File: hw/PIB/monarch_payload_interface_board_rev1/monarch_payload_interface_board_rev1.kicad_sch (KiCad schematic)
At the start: 0 parts

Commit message: Components selection for valves so far
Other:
- added sheet MCU (MCU.kicad_sch)
- added sheet PC104_stack (PC104_stack.kicad_sch)
- added sheet Valves (valves.kicad_sch)
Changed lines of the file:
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@@
 	(generator_version "9.0")
 	(paper "A4")
+	(sheet
+		(at 106.68 52.07)
+		(size 111.76 17.78)
+		(exclude_from_sim no)
+		(in_bom yes)
+		(on_board yes)
+		(dnp no)
+		(stroke
+			(width 0.1524)
+			(type solid)
+		)
+		(fill
+			(color 0 0 0 0.0000)
+		)
+		(property "Sheetname" "MCU"
+			(at 106.68 51.3584 0)
+			(effects
+				(font
+					(size 1.27 1.27)
+				)
+				(justify left bottom)
+			)
+		)
+		(property "Sheetfile" "MCU.kicad_sch"
+			(at 113.284 50.038 0)
+			(effects
+				(font
+					(size 1.27 1.27)
+				)
+				(justify left top)
+			)
+		)
+		(instances
+			(project "monarch_payload_interface_board_rev1"
+				(path "/bf7ee58d-ac53-49d1-a6b2-96a87d67b737"
+					(page "3")
+				)
+			)
+		)
+	)
+	(sheet
+		(at 62.23 52.07)
+		(size 34.29 80.01)
+		(exclude_from_sim no)
+		(in_bom yes)
+		(on_board yes)
+		(dnp no)
+		(fields_autoplaced yes)
+		(stroke
+			(width 0.1524)
+			(type solid)
+		)
+		(fill
+			(color 0 0 0 0.0000)
+		)
+		(property "Sheetname" "PC104_stack"
+			(at 62.23 51.3584 0)
+			(effects
+				(font
+					(size 1.27 1.27)
+				)
+				(justify left bottom)
+			)
+		)
+		(property "Sheetfile" "PC104_stack.kicad_sch"
+			(at 62.23 132.6646 0)
+			(effects
+				(font
+					(size 1.27 1.27)
+				)
+				(justify left top)
+			)
+		)
+		(instances
+			(project "monarch_payload_interface_board_rev1"
+				(path "/bf7ee58d-ac53-49d1-a6b2-96a87d67b737"
+					(page "2")
+				)
+			)
+		)
+	)
+	(sheet
+		(at 125.73 92.71)
+		(size 72.39 34.29)
+		(exclude_from_sim no)
+		(in_bom yes)
+		(on_board yes)
+		(dnp no)
+		(fields_autoplaced yes)
+		(stroke
+			(width 0.1524)
+			(type solid)
+		)
+		(fill
+			(color 0 0 0 0.0000)
+		)
+		(property "Sheetname" "Valves"
+			(at 125.73 91.9984 0)
+			(effects
+				(font
+					(size 1.27 1.27)
+				)
+				(justify left bottom)
+			)
+		)
+		(property "Sheetfile" "valves.kicad_sch"
+			(at 125.73 127.5846 0)
+			(effects
+				(font
+					(size 1.27 1.27)
+				)
+				(justify left top)
+			)
+		)
+		(instances
+			(project "monarch_payload_interface_board_rev1"
+				(path "/bf7ee58d-ac53-49d1-a6b2-96a87d67b737"
+					(page "4")
+				)
+			)
+		)
+	)
 	(sheet_instances
 		(path "/"

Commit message: More components
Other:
- added sheet 12V Power Supply (power supply.kicad_sch)
- added sheet TCs (thermocouples.kicad_sch)
- sheet MCU ports: added 3V3, GND, I2C1_SCL, I2C1_SDA, I2C2_SCL, I2C2_SDA, I2C3_SCL, I2C3_SDA, I2C4_SCL, I2C4_SDA, SPI3_MISO, SPI3_MOSI, SPI3_SCK, UART_RX, UART_TX, Valve1, Valve10, Valve11, Valve12, Valve13, Valve14, Valve15, Valve16, Valve17, Valve18, Valve2, Valve3, Valve4, Valve5, Valve6, Valve7, Valve8, Valve9; removed none
- sheet PC104_stack ports: added 12VA, 3V3, 5V, GND, UART_RX, UART_TX, VBAT; removed none
- sheet Valves ports: added 12VA, 12VB, 3V3, GND, Valve1, Valve1+, Valve1-, Valve2, Valve2+, Valve2-, Valve3; removed none

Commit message: Schematic Review
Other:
- sheet PC104_stack renamed PC104 Stack
- added sheet Connectors (connectors.kicad_sch)
- added sheet Heater (heater.kicad_sch)
- added sheet PTs (pts.kicad_sch)
- sheet MCU ports: added Heater0, PT, T1, T2, T3, T4, T5; removed none
- sheet TCs ports: added T0+, T0-, T1, T2, T2+, T2-, T3, T3+, T3-, T4, T4+, T4-, T5; removed none
- sheet Valves ports: added Valve10, Valve10+, Valve10-, Valve11, Valve11+, Valve11-, Valve12, Valve12+, Valve12-, Valve13, Valve13+, Valve13-, Valve14, Valve14+, Valve14-, Valve15, Valve15+, Valve15-, Valve16, Valve16+, Valve16-, Valve17, Valve17+, Valve17-, Valve18, Valve18+, Valve18-, Valve3+, Valve3-, Valve4, Valve4+, Valve4-, Valve5, Valve5+, Valve5-, Valve6, Valve6+, Valve6-, Valve7, Valve7+, Valve7-, Valve8, Valve8+, Valve8-, Valve9, Valve9+, Valve9-; removed none

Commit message: PCB updates
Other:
- sheet 12V Power Supply ports: added +12VB, EN; removed 12VB
- sheet Connectors ports: added +3V3; removed 3V3
- sheet Heater ports: added +12VA; removed 12VA
- sheet MCU ports: added +3V3, ADC, EN, NRST, SPI1_MISO, SPI1_MOSI, SPI1_SCK; removed 3V3
- sheet PC104 Stack ports: added +12VA, +12VB, +3V3, ADC, NRST, SPI1_MISO, SPI1_MOSI, SPI1_SCK; removed 12VA, 3V3, 5V
- sheet PTs ports: added +12VA; removed 12VA
- sheet Valves ports: added +12VA, +12VB; removed 12VA, 12VB

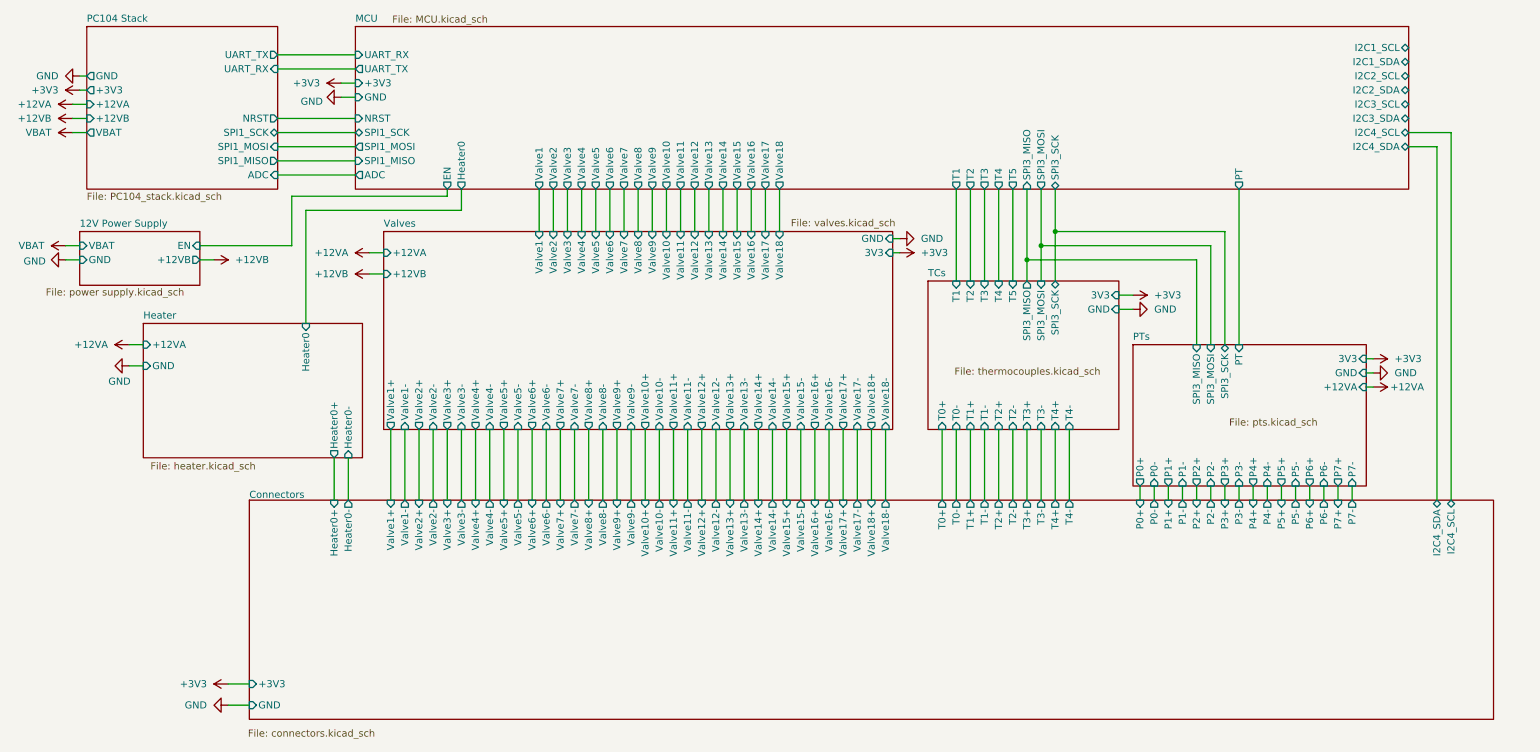
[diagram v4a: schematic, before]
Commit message: PIB layout update
done pending Ben O approval
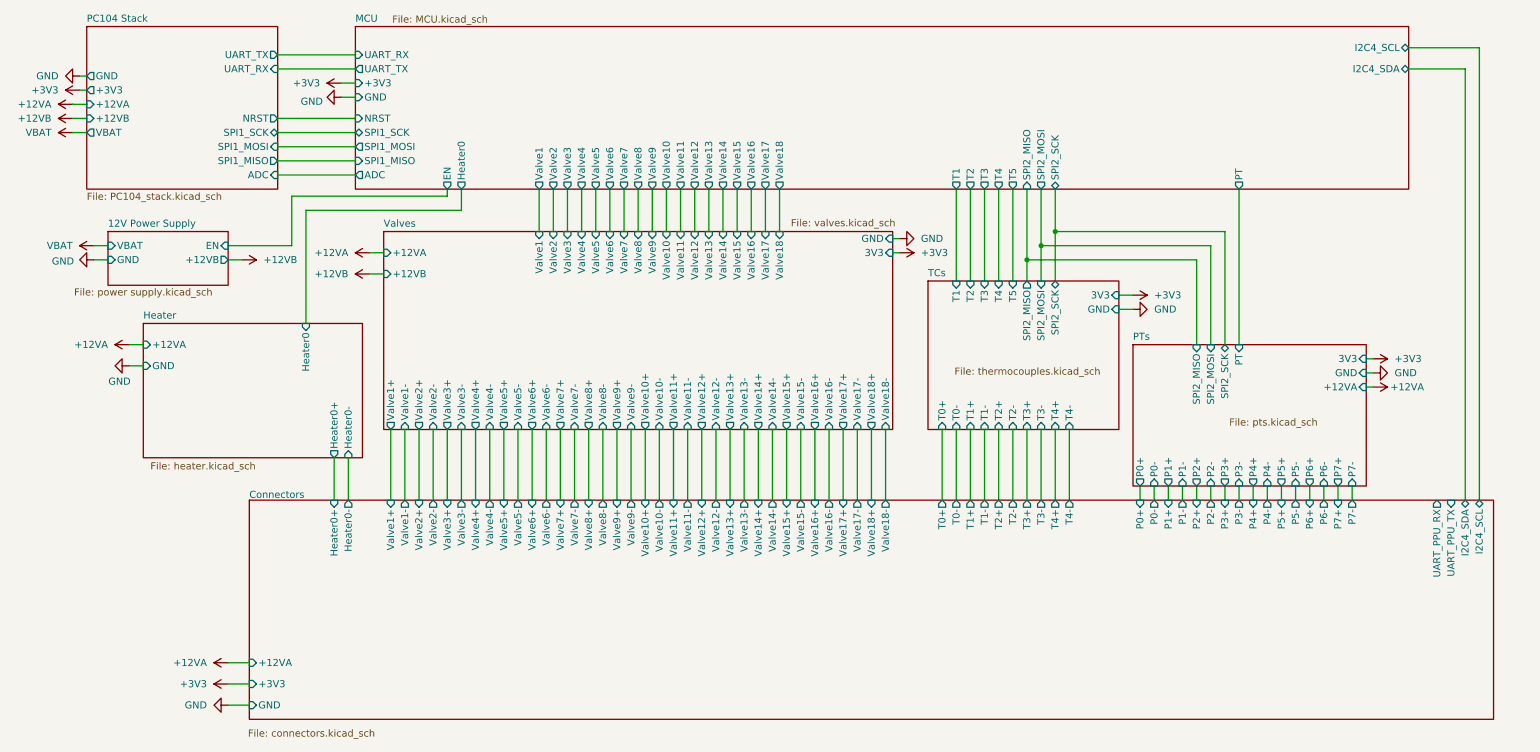
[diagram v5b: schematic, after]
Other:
- sheet Connectors ports: added +12VA, UART_PPU_RX, UART_PPU_TX; removed none
- sheet MCU ports: added SPI2_MISO, SPI2_MOSI, SPI2_SCK; removed I2C1_SCL, I2C1_SDA, I2C2_SCL, I2C2_SDA, I2C3_SCL, I2C3_SDA, SPI3_MISO, SPI3_MOSI, SPI3_SCK
- sheet PTs ports: added SPI2_MISO, SPI2_MOSI, SPI2_SCK; removed SPI3_MISO, SPI3_MOSI, SPI3_SCK
- sheet TCs ports: added SPI2_MISO, SPI2_MOSI, SPI2_SCK; removed SPI3_MISO, SPI3_MOSI, SPI3_SCK

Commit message: PIB minor updates & radio board
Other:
- sheet MCU ports: added UART4_RX, UART4_TX, USART3_RX, USART3_TX; removed UART_RX, UART_TX
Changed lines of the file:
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@@
 	(wire
 		(pts
+			(xy 262.89 30.48) (xy 267.97 30.48)
+		)
+		(stroke
+			(width 0)
+			(type default)
+		)
+	)
+	(wire
+		(pts
 			(xy 237.49 100.33) (xy 237.49 102.87)
 		)
@@
 	(wire
 		(pts
+			(xy 270.51 27.94) (xy 270.51 102.87)
+		)
+		(stroke
+			(width 0)
+			(type default)
+		)
+	)
+	(wire
+		(pts
 			(xy 229.87 54.61) (xy 229.87 74.93)
 		)
@@
 	(wire
 		(pts
+			(xy 267.97 30.48) (xy 267.97 102.87)
+		)
+		(stroke
+			(width 0)
+			(type default)
+		)
+	)
+	(wire
+		(pts
 			(xy 245.11 100.33) (xy 245.11 102.87)
 		)
@@
 	(wire
 		(pts
+			(xy 262.89 27.94) (xy 270.51 27.94)
+		)
+		(stroke
+			(width 0)
+			(type default)
+		)
+	)
+	(wire
+		(pts
 			(xy 181.61 46.99) (xy 181.61 63.5)
 		)
@@
 			)
 		)
-		(pin "UART_RX" input
-			(at 73.66 22.86 180)
-			(effects
-				(font
-					(size 1.27 1.27)
-				)
-				(justify left)
-			)
-		)
-		(pin "UART_TX" output
-			(at 73.66 25.4 180)
-			(effects
-				(font
-					(size 1.27 1.27)
-				)
-				(justify left)
-			)
-		)
 		(pin "GND" input
 			(at 73.66 30.48 180)
@@
 			)
 		)
+		(pin "UART4_TX" output
+			(at 262.89 30.48 0)
+			(effects
+				(font
+					(size 1.27 1.27)
+				)
+				(justify right)
+			)
+		)
+		(pin "USART3_RX" input
+			(at 73.66 22.86 180)
+			(effects
+				(font
+					(size 1.27 1.27)
+				)
+				(justify left)
+			)
+		)
+		(pin "USART3_TX" output
+			(at 73.66 25.4 180)
+			(effects
+				(font
+					(size 1.27 1.27)
+				)
+				(justify left)
+			)
+		)
+		(pin "UART4_RX" input
+			(at 262.89 27.94 0)
+			(effects
+				(font
+					(size 1.27 1.27)
+				)
+				(justify right)
+			)
+		)
 		(instances
 			(project "monarch_payload_interface_board_rev1"
@@
 			)
 		)
-		(pin "UART_PPU_RX" output
+		(pin "UART_PPU_RX" input
 			(at 267.97 102.87 90)
 			(effects
@@
 			)
 		)
-		(pin "UART_PPU_TX" input
+		(pin "UART_PPU_TX" output
 			(at 270.51 102.87 90)
 			(effects
